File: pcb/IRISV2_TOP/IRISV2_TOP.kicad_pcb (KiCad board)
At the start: 6 copper layers, 50 x 50 mm, 159 parts, among them IC1 ATA6561-GAQW-N, IC2 S25FL256LAGNFI010, IC3 STM32C552MET6, J1 Conn_01x20_MountingPin, J10 Conn_02x04_Odd_Even, J2 USB_C_Receptacle_USB2.0_16P, J3 USB_C_Receptacle_USB2.0_16P, J5 Conn_02x04_Odd_Even, J6 MEM2085-00-115-00-A, J7 Conn_Coaxial, J8 Conn_Coaxial, J9 Conn_01x06_MountingPin, U4 STM32H563VITx, U5 MMC5983MA, U6 ICM-45686, U7 ICM-45686, U8 BMP581, U9 lr2021, Y1 25mHz 8pf, Y2 32.768kHz 12.5pF, Y3 24mHz 8pf, Y4 32.768kHz 12.5pF, Y5 ECS-TXO-32CSMV-320-AN-TR

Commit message: lr2021 reroute, maybe need to do stuff with gps lna bc iip3 and ip1db
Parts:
- moved C56 2.94 mm to (150.3, 106.7), turned to 180 degrees
- moved C89 1.06 mm to (153.9, 119.6)
- moved C54 0.50 mm to (153.3, 109.2)
- moved C55 0.50 mm to (147.6, 109.2)
- moved C59 0.50 mm to (145.6, 108.7)
- moved J7 0.50 mm to (141.4, 113.0)
- moved J8 0.50 mm to (141.4, 119.0)
- moved U5 0.50 mm to (150.0, 109.0)
- moved C71 0.40 mm to (155.8, 111.0)
- moved C77 0.40 mm to (152.9, 111.0)
- moved C79 0.40 mm to (150.2, 112.0)
- moved C84 0.40 mm to (155.8, 120.5)
- moved D7 0.40 mm to (146.4, 113.0)
- moved D8 0.40 mm to (145.6, 118.5)
- moved L10 0.40 mm to (155.8, 118.6)
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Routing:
- net GND: track 68.3 -> 58.3 mm, vias 205 -> 200
- net /lr2021/lf: track 10.5 -> 11.8 mm
- net +3.3V: track 66.7 -> 66.1 mm, vias 27 -> 26

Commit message: most routing done inc some reassignment, pretty much just connectors left now
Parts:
- removed C3: 1uF, Capacitor_SMD:C_0603_1608Metric
- R12, R13, R14: moved to F.Cu
- moved C2 50.7 mm to (143.4, 109.2), turned to 90 degrees
- moved C4 47.1 mm to (145.2, 110.0)
- moved D5 43.5 mm to (149.0, 95.2), turned to -90 degrees
- moved R19 43.4 mm to (149.8, 92.8), turned to 180 degrees
- moved R9 38.2 mm to (142.1, 105.0), turned to 0 degrees
- moved D6 35.1 mm to (151.0, 95.2), turned to -90 degrees
- moved R28 33.1 mm to (152.8, 95.6), turned to 90 degrees
- moved R10 20.5 mm to (158.1, 99.4)
- moved R16 19.9 mm to (157.9, 105.0)
- moved R14 14.7 mm to (166.2, 87.6), turned to -90 degrees
- moved R12 13.2 mm to (165.2, 87.6), turned to -90 degrees
- moved R13 12.0 mm to (167.7, 88.0)
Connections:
- IC3 pad 33: /peripheral_mcu/sd_cs -> unconnected-(IC3-PE7-Pad33)
- IC3 pad 77: unconnected-(IC3-PE0-Pad77) -> /peripheral_mcu/sd_cs
- U4 pad 29: unconnected-(U4-PA4-Pad29) -> icm2_cs
- U4 pad 33: icm2_cs -> icm2_int
- U4 pad 34: icm2_int -> unconnected-(U4-PC5-Pad34)
- U4 pad 45: icm1_int -> icm_fsync
- U4 pad 46: icm1_cs -> unconnected-(U4-PE15-Pad46)
- U4 pad 47: mpu_i2c2_scl -> unconnected-(U4-PB10-Pad47)
- U4 pad 51: mpu_i2c2_sda -> icm1_cs
- U4 pad 57: unconnected-(U4-PD10-Pad57) -> icm1_int
- U4 pad 60: icm_fsync -> unconnected-(U4-PD13-Pad60)
- U4 pad 77: unconnected-(U4-PA15(JTDI)-Pad77) -> bmp_cs
- U4 pad 83: /main_mcu/can_stby -> bmp_int
- U4 pad 84: bmp_cs -> /main_mcu/can_stby
- U4 pad 85: bmp_int -> unconnected-(U4-PD4-Pad85)
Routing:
- net +5VP: track 0.00 -> 45.9 mm, vias 0 -> 6
- net gps_mrx: track 0.00 -> 32.8 mm, vias 0 -> 2
- net gps_mtx: track 0.00 -> 32.3 mm, vias 0 -> 2
- net lr_irq1: track 0.00 -> 30.4 mm, vias 0 -> 2
- net lr_irq2: track 0.00 -> 29.7 mm, vias 0 -> 2
- net lr_busy: track 0.00 -> 28.0 mm, vias 0 -> 2
- net /main_mcu/boot: track 2.39 -> 28.3 mm, vias 0 -> 2
- net lr_mosi: track 0.00 -> 25.6 mm
- net /peripheral_mcu/flash_mosi: track 7.41 -> 32.8 mm, vias 1 -> 2
- net lr_sck: track 0.00 -> 24.5 mm
- net mag_cs: track 2.29 -> 26.6 mm, vias 1 -> 2
- net /peripheral_mcu/flash_clk: track 9.28 -> 33.4 mm, vias 1 -> 2
- net /main_mcu/swclk: track 0.00 -> 23.0 mm, vias 0 -> 1
- net /peripheral_mcu/rst: track 3.41 -> 25.5 mm, vias 0 -> 2
- net mag_int: track 2.74 -> 24.8 mm, vias 1 -> 2
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- added copper zone on In3.Cu, net GND

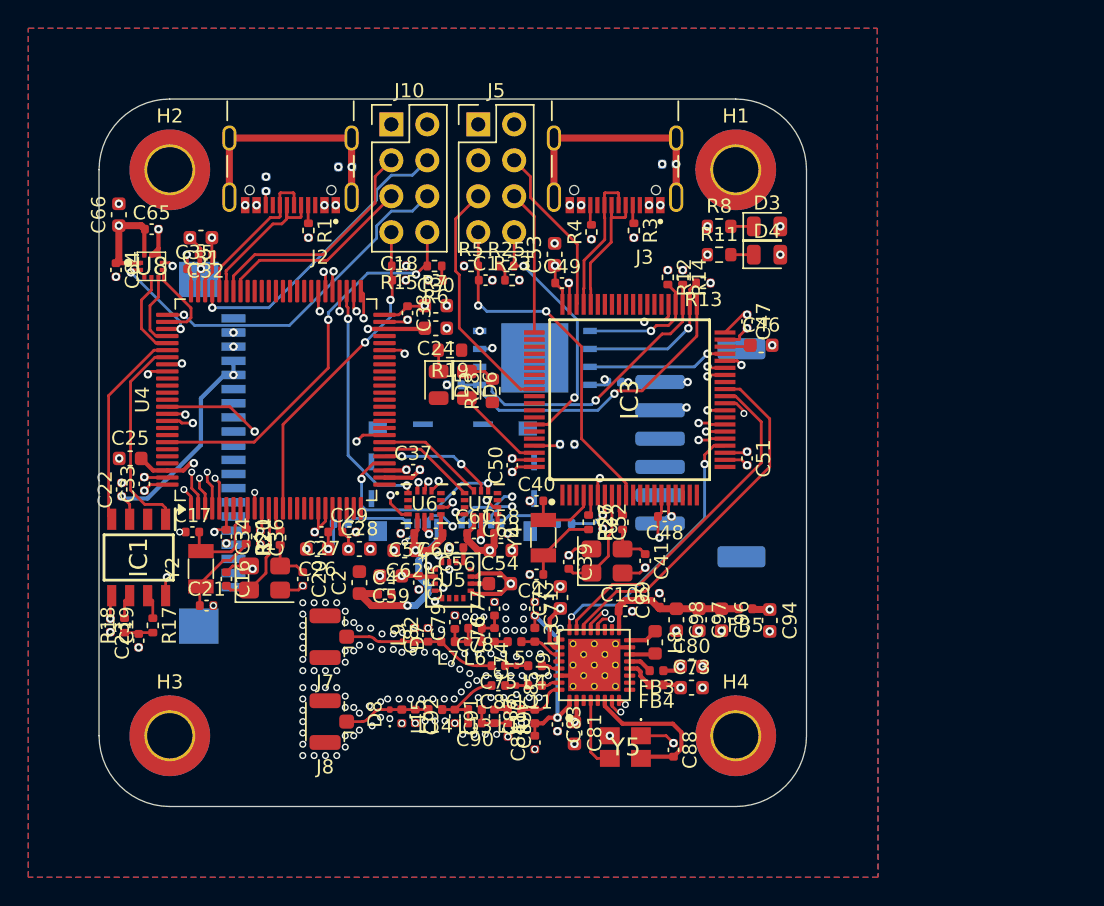
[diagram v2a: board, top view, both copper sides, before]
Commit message: all main routing done, need to break out remaining gpio onto banks of mpu and ppu
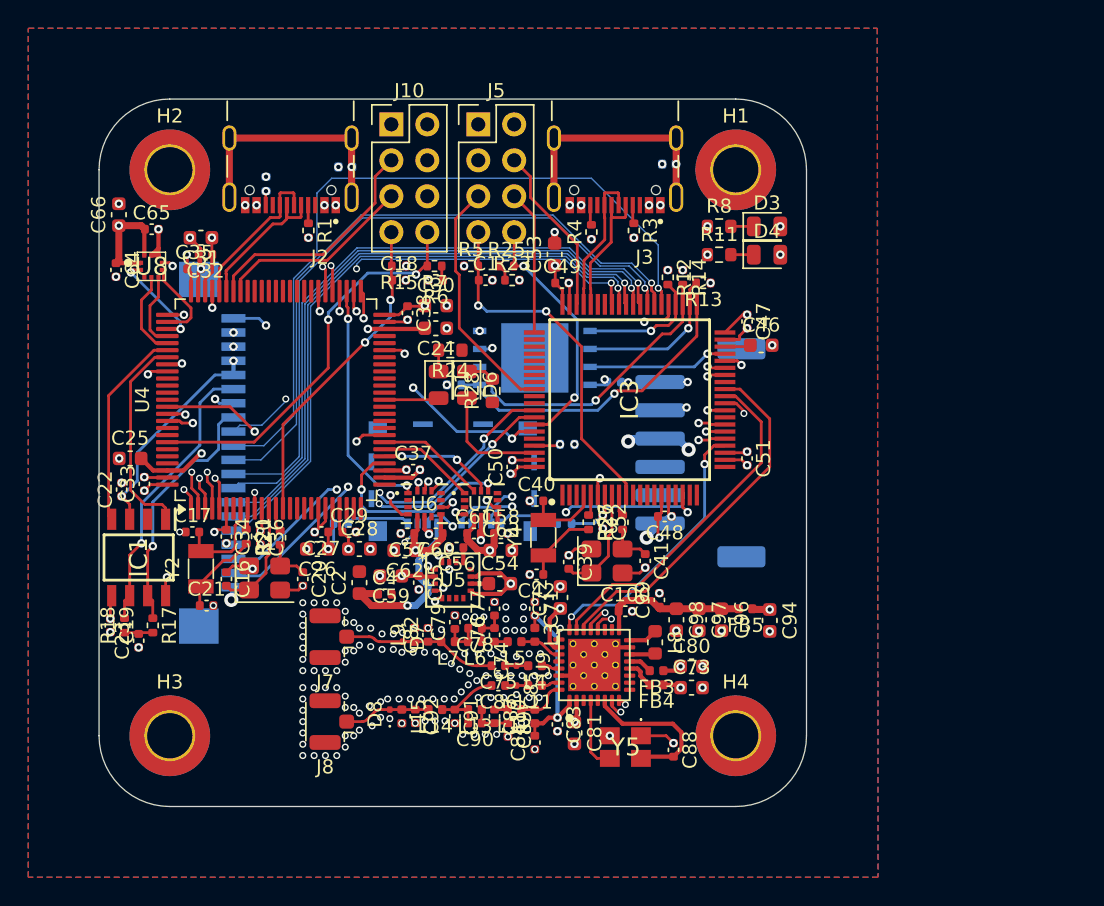
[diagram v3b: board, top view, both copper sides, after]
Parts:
- removed D5: STATUS, LED_SMD:LED_0805_2012Metric
- removed R19: 120, Resistor_SMD:R_0603_1608Metric
- added D1: STATUS, LED_SMD:LED_0805_2012Metric, F.Cu at (149.0, 95.2)
- added R24: 120, Resistor_SMD:R_0603_1608Metric, F.Cu at (149.8, 92.8)
- moved C50 0.12 mm to (154.2, 101.0)
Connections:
- IC1 pad 6: /main_mcu/can_l -> can_l
- IC1 pad 7: /main_mcu/can_h -> can_h
- IC3 pad 75: unconnected-(IC3-PB8-Pad75) -> buzzer
- J1 pad 13: GND -> can_h
- J1 pad 15: GND -> can_l
- R17 pad 1: /main_mcu/can_h -> can_h
- R18 pad 2: /main_mcu/can_l -> can_l
- U4 pad 38: unconnected-(U4-PE7-Pad38) -> Net-(D1-A)
- U4 pad 97: Net-(D5-A) -> unconnected-(U4-PE0-Pad97)
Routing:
- net cont_test: track 0.00 -> 53.2 mm, vias 0 -> 3
- net camera_enable: track 0.00 -> 52.4 mm, vias 0 -> 1
- net c5_fire: track 0.00 -> 47.4 mm, vias 0 -> 1
- net c6_fire: track 0.00 -> 46.3 mm, vias 0 -> 1
- net c4_fire: track 0.00 -> 44.6 mm, vias 0 -> 1
- net c3_fire: track 0.00 -> 44.5 mm, vias 0 -> 1
- net c2_fire: track 0.00 -> 44.3 mm, vias 0 -> 1
- net c1_fire: track 0.00 -> 44.0 mm, vias 0 -> 1
- net +5V: track 16.4 -> 58.5 mm
- net arm: track 0.00 -> 36.9 mm, vias 0 -> 3
- net ina_scl: track 0.00 -> 28.0 mm, vias 0 -> 3
- net ina_sda: track 0.00 -> 26.4 mm, vias 0 -> 3
- net buzzer: track 0.00 -> 25.0 mm, vias 0 -> 3
- net can_l: track 0.00 -> 20.2 mm, vias 0 -> 1
- net can_h: track 0.00 -> 17.7 mm, vias 0 -> 1
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
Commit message: fixed some issues, lr2021 matching is now 0201 - todo change trace width to match pad width like ref design, see todo for rest
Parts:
- removed Y5: ECS-TXO-32CSMV-320-AN-TR, ECS-TXO-32CSMV-320-AN:ECSTXO32CSMV320ANTR
- added U1: ~, ECS-TXO-20CSMV4:ECS-TXO-20CSMV4, F.Cu at (160.8, 119.8)
- C71, C75, C76, C77, C78, C79, C82, C84, C86, C87, C89, C90, C91, C92: footprint Capacitor_SMD:C_0402_1005Metric -> Capacitor_SMD:C_0201_0603Metric
- L10, L11, L12, L13, L14, L15, L4, L5, L6, L7, L9: footprint Inductor_SMD:L_0402_1005Metric -> Inductor_SMD:L_0201_0603Metric
- moved J7 3.64 mm to (144.9, 114.0)
- moved J8 3.50 mm to (144.9, 119.0)
- moved C88 3.02 mm to (162.8, 119.9), turned to 90 degrees
- moved D8 2.44 mm to (147.9, 118.0)
- moved L15 2.33 mm to (148.7, 118.0)
- moved D7 2.20 mm to (148.6, 113.5)
- moved L9 2.09 mm to (149.3, 113.5)
- moved C92 2.09 mm to (149.3, 118.0)
- moved C82 1.85 mm to (150.0, 113.5)
- moved L14 1.72 mm to (150.4, 117.7)
- moved L7 1.48 mm to (151.1, 113.8)
- moved C91 1.48 mm to (151.5, 118.0)
- moved C79 1.46 mm to (151.4, 112.7)
- moved C90 1.23 mm to (152.6, 118.4)
- moved C77 1.22 mm to (153.6, 112.1)
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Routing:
- net /lr2021/lr_vtcxo: track 10.9 -> 3.26 mm
- net /lr2021/lr_xtalin: track 5.19 -> 1.75 mm
- net /lr2021/lf: track 11.8 -> 8.54 mm
- net GND: track 65.0 -> 62.5 mm, vias 202 -> 162
- net /lr2021/hf_tiein: track 5.98 -> 4.45 mm
- net /lr2021/hf: track 6.08 -> 4.84 mm
- net Net-(C87-Pad2): track 2.80 -> 2.16 mm
- net Net-(C78-Pad2): track 2.78 -> 2.21 mm
- net Net-(C76-Pad2): track 2.76 -> 2.23 mm

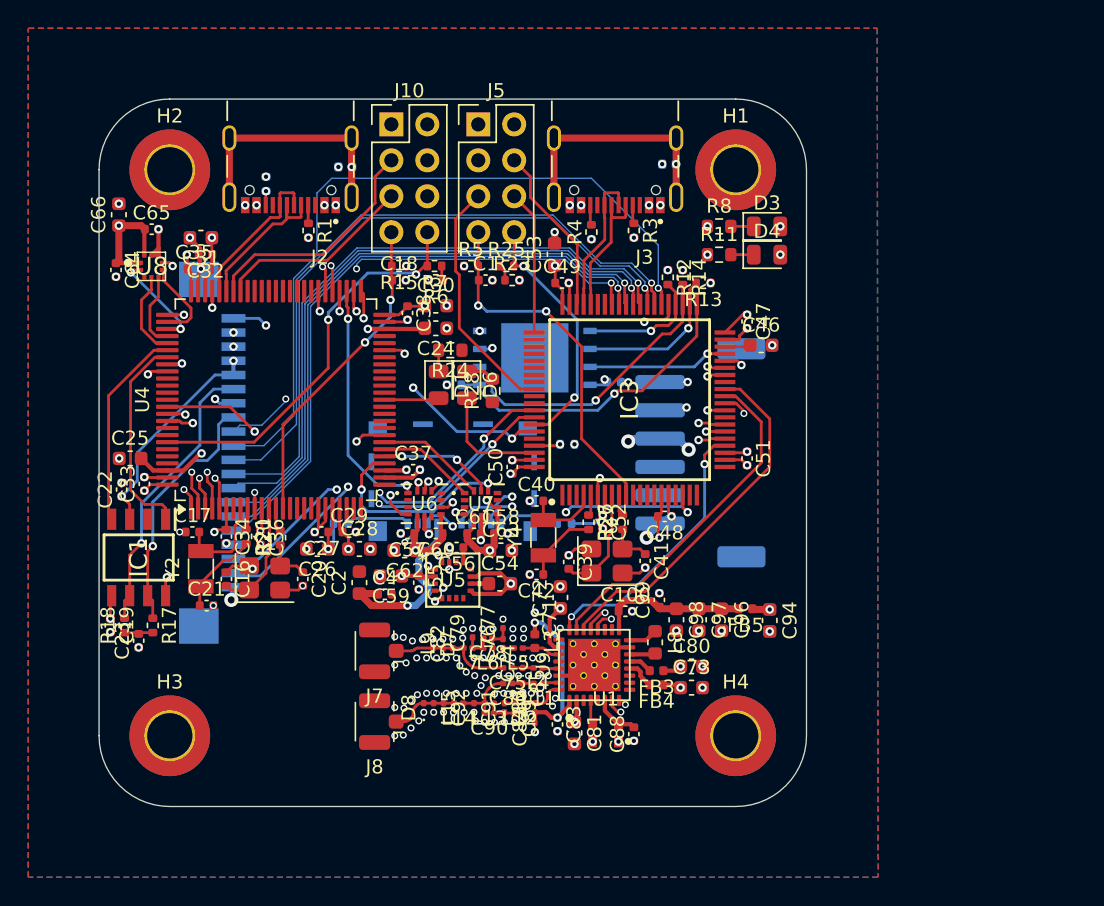
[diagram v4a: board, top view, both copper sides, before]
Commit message: removed usb, added connectors and stuff, 3d models mostly added, still need to route out gpio and servos (though connectors added)
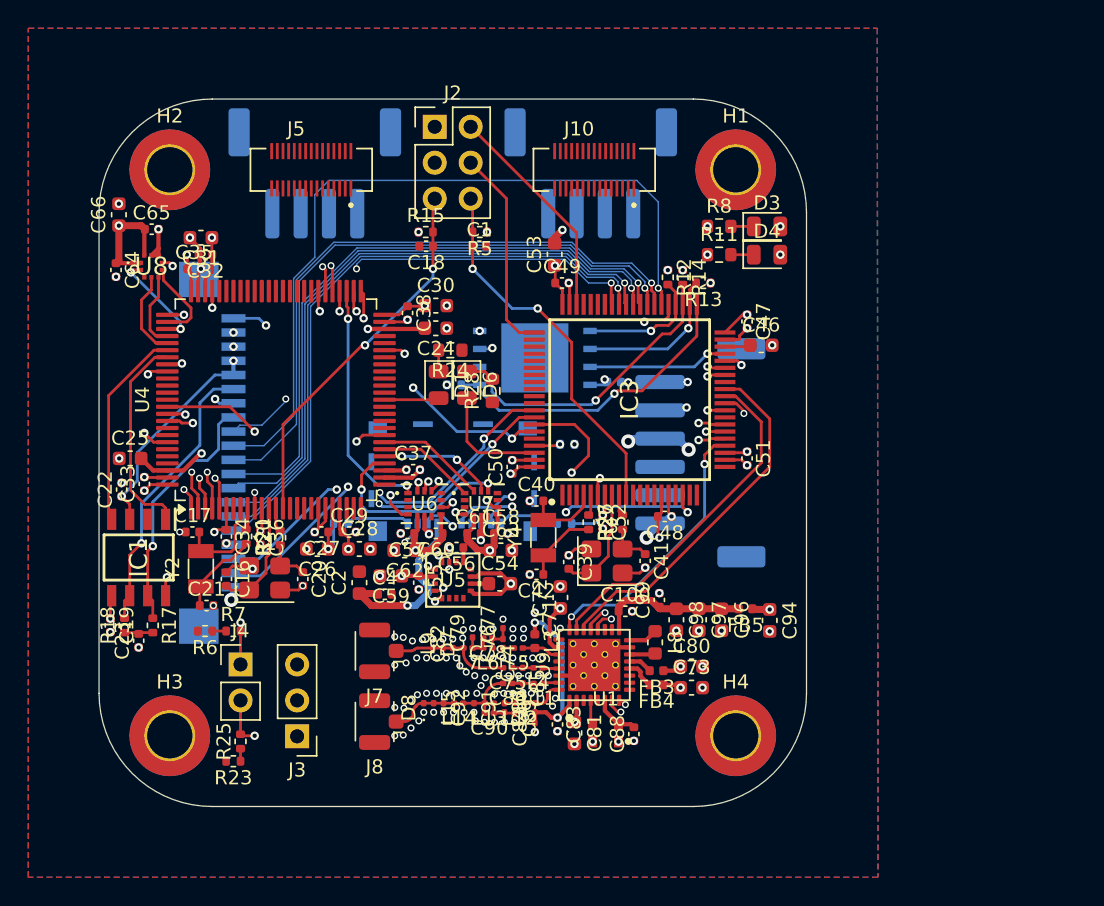
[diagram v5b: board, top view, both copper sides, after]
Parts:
- removed FB1, FB2: FerriteBead_Small, Inductor_SMD:L_0402_1005Metric
- removed R1, R2, R3, R4: 5.1k, Resistor_SMD:R_0402_1005Metric
- added J11: Conn_01x04_MountingPin, Connector_JST:JST_PH_S4B-PH-SM4-TB_1x04-1MP_P2.00mm_Horizontal, B.Cu at (140.2, 80.2)
- added J12: Conn_01x04_MountingPin, Connector_JST:JST_PH_S4B-PH-SM4-TB_1x04-1MP_P2.00mm_Horizontal, B.Cu at (159.8, 80.2)
- added J4: Conn_01x02, Connector_PinHeader_2.54mm:PinHeader_1x02_P2.54mm_Vertical, F.Cu at (135.0, 115.0)
- J10, J5: value Conn_02x04_Odd_Even -> Conn_02x15_Odd_Even; footprint Connector_PinHeader_2.54mm:PinHeader_2x04_P2.54mm_Vertical -> 10164227-0304A1RLF:AMPHENOL_10164227-0305A1RLF
- J2: value USB_C_Receptacle_USB2.0_16P -> Conn_02x03_Odd_Even; footprint UJ20-C-H-G-SMT-1-P16-TR:SAMESKY_UJ20-C-H-G-SMT-1-P16-TR -> Connector_PinHeader_2.54mm:PinHeader_2x03_P2.54mm_Vertical
- J3: value USB_C_Receptacle_USB2.0_16P -> Conn_01x03; footprint UJ20-C-H-G-SMT-1-P16-TR:SAMESKY_UJ20-C-H-G-SMT-1-P16-TR -> Connector_PinHeader_2.54mm:PinHeader_1x03_P2.54mm_Vertical
- moved J3 50.2 mm to (139.0, 120.0)
- moved R23 39.3 mm to (134.5, 121.8), turned to 180 degrees
- moved R25 38.5 mm to (135.0, 120.4), turned to 90 degrees
- moved R6 29.7 mm to (132.5, 112.6)
- moved R7 29.5 mm to (134.5, 112.6), turned to 0 degrees
- moved J10 14.7 mm to (160.0, 80.0)
- moved J5 12.2 mm to (140.0, 80.0)
- moved J2 10.4 mm to (148.7, 77.0), turned to 0 degrees
- moved C18 3.07 mm to (148.1, 85.4), turned to 180 degrees
- moved R15 3.05 mm to (148.1, 84.4), turned to 0 degrees
- moved R5 2.48 mm to (151.9, 84.4), turned to 180 degrees
- moved C1 2.44 mm to (151.9, 85.4)
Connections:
- C1 pad 1: /peripheral_mcu/rst -> ppu_rst
- C18 pad 1: /main_mcu/rst -> mcu_rst
- IC3 pad 10: /peripheral_mcu/rst -> ppu_rst
- IC3 pad 58: /peripheral_mcu/swdio -> ppu_swdio
- IC3 pad 61: /peripheral_mcu/swclk -> ppu_swclk
- IC3 pad 74: /peripheral_mcu/boot -> ppu_boot
- J10 pad 1: GND -> unconnected-(J10-Pin_1-Pad1)
- J10 pad 2: +3.3V -> unconnected-(J10-Pin_2-Pad2)
- J10 pad 3: /main_mcu/debug_uart_rx -> unconnected-(J10-Pin_3-Pad3)
- J10 pad 4: /main_mcu/swdio -> unconnected-(J10-Pin_4-Pad4)
- J10 pad 5: /main_mcu/debug_uart_tx -> unconnected-(J10-Pin_5-Pad5)
- J10 pad 6: /main_mcu/swclk -> unconnected-(J10-Pin_6-Pad6)
- J10 pad 7: /main_mcu/rst -> unconnected-(J10-Pin_7-Pad7)
- J10 pad 8: /main_mcu/boot -> unconnected-(J10-Pin_8-Pad8)
- J5 pad 1: GND -> unconnected-(J5-Pin_1-Pad1)
- J5 pad 2: +3.3V -> unconnected-(J5-Pin_2-Pad2)
- J5 pad 3: GND -> unconnected-(J5-Pin_3-Pad3)
- J5 pad 4: /peripheral_mcu/swdio -> unconnected-(J5-Pin_4-Pad4)
- J5 pad 5: /peripheral_mcu/swo -> unconnected-(J5-Pin_5-Pad5)
- J5 pad 6: /peripheral_mcu/swclk -> unconnected-(J5-Pin_6-Pad6)
- J5 pad 7: /peripheral_mcu/rst -> unconnected-(J5-Pin_7-Pad7)
- J5 pad 8: /peripheral_mcu/boot -> unconnected-(J5-Pin_8-Pad8)
- R15 pad 2: /main_mcu/rst -> mcu_rst
- R25 pad 2: /peripheral_mcu/boot -> ppu_boot
- R5 pad 2: /peripheral_mcu/rst -> ppu_rst
- R7 pad 2: /main_mcu/boot -> mcu_boot
- U4 pad 14: /main_mcu/rst -> mcu_rst
- U4 pad 23: pwm5 -> /main_mcu/pwm5
- U4 pad 24: pwm6 -> /main_mcu/pwm6
- U4 pad 25: pwm7 -> /main_mcu/pwm7
- U4 pad 26: pwm8 -> /main_mcu/pwm8
- U4 pad 63: pwm1 -> /main_mcu/pwm1
- U4 pad 64: pwm2 -> /main_mcu/pwm2
- U4 pad 65: pwm3 -> /main_mcu/pwm3
- U4 pad 66: pwm4 -> /main_mcu/pwm4
- U4 pad 72: /main_mcu/swdio -> mcu_swdio
- U4 pad 76: /main_mcu/swclk -> mcu_swclk
- U4 pad 94: /main_mcu/boot -> mcu_boot
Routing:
- net ppu_boot: track 0.00 -> 47.0 mm, vias 0 -> 2
- net /main_mcu/boot: track 28.3 -> 0.00 mm, vias 2 -> 0
- net ppu_rst: track 0.00 -> 26.6 mm, vias 0 -> 2
- net mcu_rst: track 0.00 -> 26.4 mm, vias 0 -> 2
- net /peripheral_mcu/rst: track 25.5 -> 0.00 mm, vias 2 -> 0
- net mcu_swclk: track 0.00 -> 23.4 mm, vias 0 -> 1
- net /main_mcu/rst: track 22.7 -> 0.00 mm, vias 2 -> 0
- net mcu_swdio: track 0.00 -> 22.2 mm, vias 0 -> 1
- net /main_mcu/swclk: track 21.8 -> 0.00 mm, vias 1 -> 0
- net /main_mcu/swdio: track 21.6 -> 0.00 mm, vias 1 -> 0
- net mcu_boot: track 0.00 -> 21.1 mm, vias 0 -> 2
- net /peripheral_mcu/boot: track 17.7 -> 0.00 mm, vias 2 -> 0
- net /peripheral_mcu/swo: track 17.2 -> 0.00 mm
- net Net-(J3-SHIELD): track 17.0 -> 0.00 mm, vias 1 -> 0
- net Net-(J2-SHIELD): track 17.0 -> 0.00 mm, vias 1 -> 0
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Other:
- outline, holes or cut-outs redrawn
